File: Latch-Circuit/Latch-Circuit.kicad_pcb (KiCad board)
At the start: 4 copper layers, 0 parts

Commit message: add footprints from sch
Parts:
- added C1: 22u, ProjectEV_Capacitor:C_3216M, F.Cu at (-17.9, -17.3)
- added C2: 10n, ProjectEV_Capacitor:C_1608M, F.Cu at (-16.1, -39.3)
- added C3: 100n, ProjectEV_Capacitor:C_1608M, F.Cu at (-16.1, -37.0)
- added C4: 10n, ProjectEV_Capacitor:C_1608M, F.Cu at (-16.1, -34.6)
- added C5: 10n, ProjectEV_Capacitor:C_1608M, F.Cu at (-16.1, -32.2)
- added C6: 10n, ProjectEV_Capacitor:C_1608M, F.Cu at (-16.1, -29.9)
- added C7: 1n, ProjectEV_Capacitor:C_3216M, F.Cu at (-17.9, -14.1)
- added D1: PZ1AH11B-AU_R1_000A1, ProjectEV_Diode:PZ1AH11B-AU_R1_000A1, F.Cu at (-17.5, -10.8)
- added D2: B1911PG--20D000514U1930, ProjectEV_LED:B1911PG--20D000514U1930, F.Cu at (-41.5, -15.3)
- added D3: CUHZ20V,H3F, ProjectEV_Protection:CUHZ20V,H3F, F.Cu at (-45.8, -15.1)
- added F1: 0ABB-1000-TM, ProjectEV_Fuse:0ABB-1000-TM, F.Cu at (-46.6, -12.3)
- added H1: MountingHole_4.3mm_M4_Pad_Via, ProjectEV_Mechanical:MountingHole_4.3mm_M4_Pad_Via, F.Cu at (-53.3, -53.0)
- added H2: MountingHole_4.3mm_M4_Pad_Via, ProjectEV_Mechanical:MountingHole_4.3mm_M4_Pad_Via, F.Cu at (-53.3, -42.8)
- added H3: MountingHole_4.3mm_M4_Pad_Via, ProjectEV_Mechanical:MountingHole_4.3mm_M4_Pad_Via, F.Cu at (-53.3, -32.7)
- added H4: MountingHole_4.3mm_M4_Pad_Via, ProjectEV_Mechanical:MountingHole_4.3mm_M4_Pad_Via, F.Cu at (-53.3, -22.5)
- added J1: 2-1445052-2, ProjectEV_Connector:2-1445052-2, F.Cu at (-24.0, -21.6)
- added J2: 3-794633-8, ProjectEV_Connector:3-794633-8, F.Cu at (-22.9, -51.3)
- added J3: B2P-VH, ProjectEV_Connector_JST:B2P-VH, F.Cu at (-27.6, -14.4)
- added J4: 3-794633-6, ProjectEV_Connector:3-794633-6, F.Cu at (-31.4, -33.7)
- added Q1: DMP3098LQ-7, ProjectEV_Transistor:DMP3098LQ-7, F.Cu at (-37.0, -24.7)
- added Q2: 2N7002K-AU_R1_000A2, ProjectEV_Transistor:2N7002K-AU_R1_000A2, F.Cu at (-37.0, -20.2)
- added Q3: 2N7002K-AU_R1_000A2, ProjectEV_Transistor:2N7002K-AU_R1_000A2, F.Cu at (-37.0, -15.8)
- added Q4: 2N7002K-AU_R1_000A2, ProjectEV_Transistor:2N7002K-AU_R1_000A2, F.Cu at (-37.0, -11.3)
- added Q5: 2N7002K-AU_R1_000A2, ProjectEV_Transistor:2N7002K-AU_R1_000A2, F.Cu at (-32.5, -24.7)
- added Q6: 2N7002K-AU_R1_000A2, ProjectEV_Transistor:2N7002K-AU_R1_000A2, F.Cu at (-32.5, -20.2)
- added Q7: 2N7002K-AU_R1_000A2, ProjectEV_Transistor:2N7002K-AU_R1_000A2, F.Cu at (-32.5, -15.8)
- added R1: 10k, ProjectEV_Resistor:R_1608M, F.Cu at (-46.2, -56.8)
- added R10: 100, ProjectEV_Resistor:R_1608M, F.Cu at (-42.2, -51.8)
- added R11: 100k, ProjectEV_Resistor:R_1608M, F.Cu at (-42.2, -49.3)
- added R12: 10k, ProjectEV_Resistor:R_1608M, F.Cu at (-42.2, -46.8)
- added R13: 100, ProjectEV_Resistor:R_1608M, F.Cu at (-42.2, -44.2)
- added R14: 100k, ProjectEV_Resistor:R_1608M, F.Cu at (-42.2, -41.7)
- added R15: 10k, ProjectEV_Resistor:R_1608M, F.Cu at (-38.2, -56.8)
- added R16: 100, ProjectEV_Resistor:R_1608M, F.Cu at (-38.2, -54.3)
- added R17: 100k, ProjectEV_Resistor:R_1608M, F.Cu at (-38.2, -51.8)
- added R18: 1.2k, ProjectEV_Resistor:R_3216M, F.Cu at (-20.8, -38.8)
- added R19: 100, ProjectEV_Resistor:R_1608M, F.Cu at (-38.2, -49.3)
- added R2: 10k, ProjectEV_Resistor:R_1608M, F.Cu at (-46.2, -54.3)
- added R20: 100k, ProjectEV_Resistor:R_1608M, F.Cu at (-38.2, -46.8)
- added R21: 1.2k, ProjectEV_Resistor:R_3216M, F.Cu at (-20.8, -35.5)
- added R22: 100, ProjectEV_Resistor:R_1608M, F.Cu at (-38.2, -44.2)
- added R23: 100k, ProjectEV_Resistor:R_1608M, F.Cu at (-38.2, -41.7)
- added R24: 1.2k, ProjectEV_Resistor:R_3216M, F.Cu at (-20.8, -32.2)
- added R25: 100, ProjectEV_Resistor:R_1608M, F.Cu at (-34.2, -56.8)
- added R26: 100k, ProjectEV_Resistor:R_1608M, F.Cu at (-34.2, -54.3)
- added R27: 1M, ProjectEV_Resistor:R_3216M, F.Cu at (-20.8, -29.0)
- added R28: 0, ProjectEV_Resistor:R_1608M, F.Cu at (-34.2, -51.8)
- added R29: 0, ProjectEV_Resistor:R_1608M, F.Cu at (-34.2, -49.3)
- added R3: 0, ProjectEV_Resistor:R_1608M, F.Cu at (-46.2, -51.8)
- added R30: 0, ProjectEV_Resistor:R_1608M, F.Cu at (-34.2, -46.8)
- added R4: 0, ProjectEV_Resistor:R_1608M, F.Cu at (-46.2, -49.3)
- added R5: 0, ProjectEV_Resistor:R_1608M, F.Cu at (-46.2, -46.8)
- added R6: 0, ProjectEV_Resistor:R_1608M, F.Cu at (-46.2, -44.2)
- added R7: 100, ProjectEV_Resistor:R_1608M, F.Cu at (-46.2, -41.7)
- added R8: 10k, ProjectEV_Resistor:R_1608M, F.Cu at (-42.2, -56.8)
- added R9: 10k, ProjectEV_Resistor:R_1608M, F.Cu at (-42.2, -54.3)
- added U1: TLP3106A(TP,F, ProjectEV_Relay:TLP3106A(TP,F, F.Cu at (-43.7, -36.4)
- added U2: TLP3106A(TP,F, ProjectEV_Relay:TLP3106A(TP,F, F.Cu at (-43.7, -28.4)
- added U3: TLP3106A(TP,F, ProjectEV_Relay:TLP3106A(TP,F, F.Cu at (-43.7, -20.4)
- added U4: CD4043BPWR, ProjectEV_Logic:CD4043BPWR, F.Cu at (-53.6, -14.1)

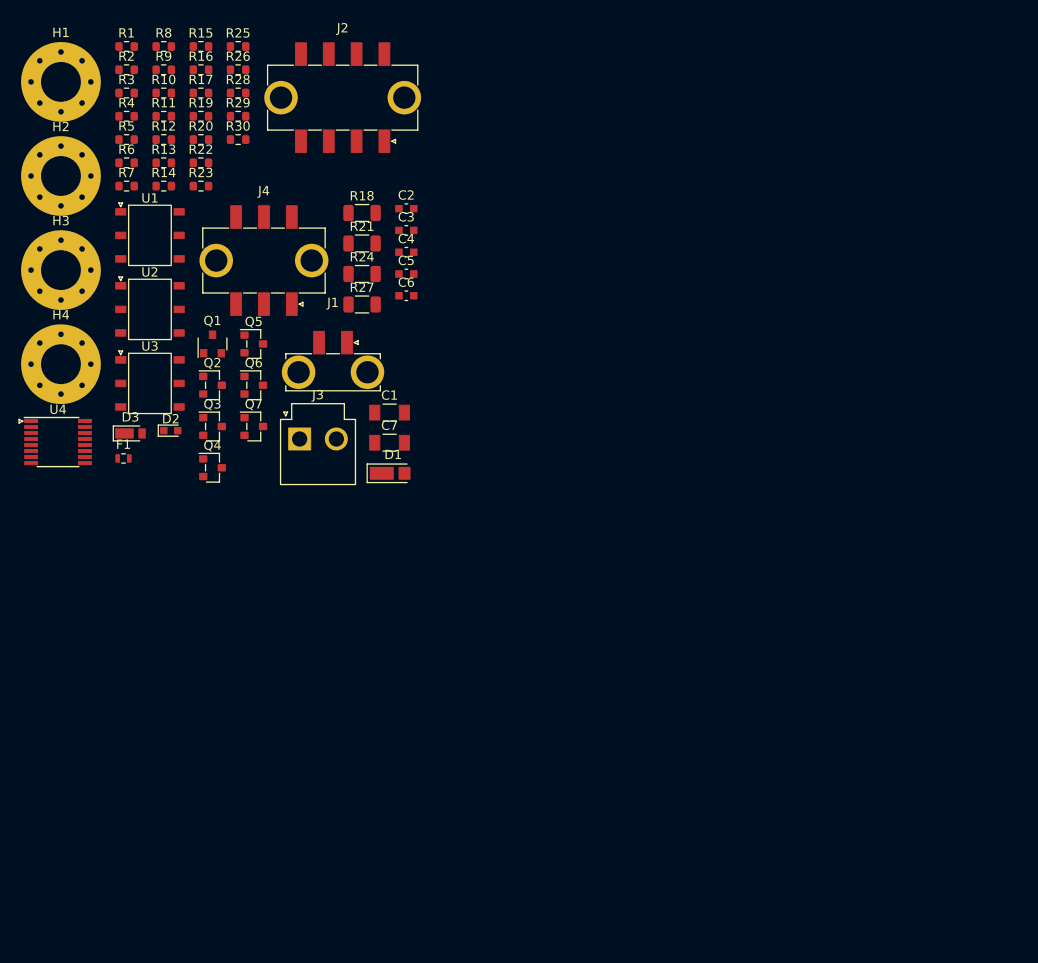
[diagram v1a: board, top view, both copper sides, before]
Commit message: update footprints, and place components
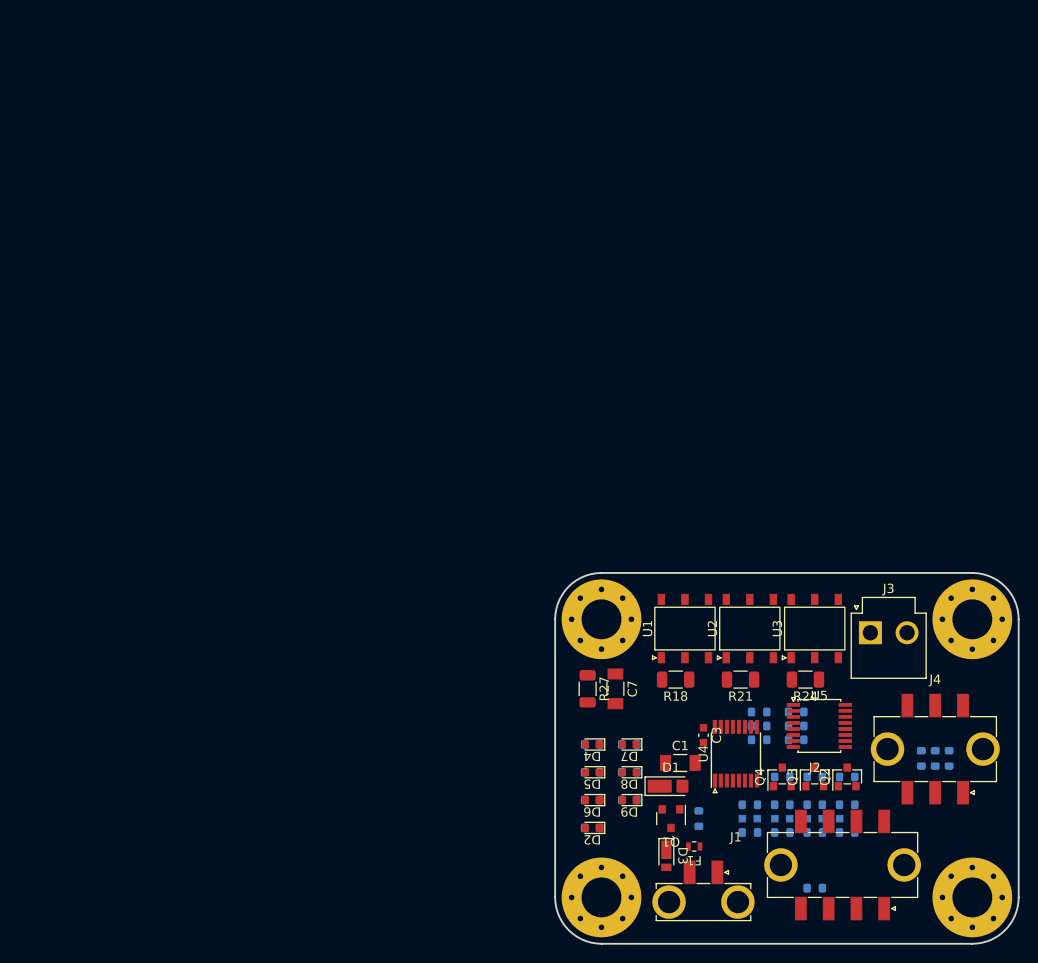
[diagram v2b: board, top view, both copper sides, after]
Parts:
- removed Q5, Q6, Q7: 2N7002K-AU_R1_000A2, ProjectEV_Transistor:2N7002K-AU_R1_000A2
- added D4: B1911PG--20D000514U1930, ProjectEV_LED:B1911PG--20D000514U1930, F.Cu at (4.00, 18.5)
- added D5: B1911PG--20D000514U1930, ProjectEV_LED:B1911PG--20D000514U1930, F.Cu at (4.00, 21.5)
- added D6: B1911PG--20D000514U1930, ProjectEV_LED:B1911PG--20D000514U1930, F.Cu at (4.00, 24.5)
- added D7: B1911USD-20D000114U1930, ProjectEV_LED:B1911USD-20D000114U1930, F.Cu at (8.00, 18.5)
- added D8: B1911USD-20D000114U1930, ProjectEV_LED:B1911USD-20D000114U1930, F.Cu at (8.00, 21.5)
- added D9: B1911USD-20D000114U1930, ProjectEV_LED:B1911USD-20D000114U1930, F.Cu at (8.00, 24.5)
- added R31: 10k, ProjectEV_Resistor:R_1608M, B.Cu at (4.00, 18.5)
- added R32: 10k, ProjectEV_Resistor:R_1608M, B.Cu at (4.00, 21.5)
- added R33: 10k, ProjectEV_Resistor:R_1608M, B.Cu at (4.00, 24.5)
- added U5: TBD62003AFNG,EL, ProjectEV_PowerManagement:TBD62003AFNG,EL, F.Cu at (28.5, 16.5)
- C2, C4, C5, C6, R1, R10, R11, R12, R13, R14, R15, R16, R17, R19, R2, R20, R22, R23, R25, R26, R3, R4, R5, R6, R7, R8, R9: moved to B.Cu
- R28, R29, R30: value 0 -> 10k; moved to B.Cu
- moved H3 119.3 mm to (45.0, 35.0)
- moved R3 114.1 mm to (42.5, 20.0), turned to 90 degrees
- moved R4 111.4 mm to (41.0, 20.0), turned to 90 degrees
- moved R5 108.7 mm to (39.5, 20.0), turned to 90 degrees
- moved R10 108.6 mm to (31.5, 28.0)
- moved R6 107.8 mm to (28.0, 34.0), turned to 180 degrees
- moved R9 106.1 mm to (31.5, 22.0), turned to 180 degrees
- moved R11 104.6 mm to (31.5, 25.0)
- moved R1 103.7 mm to (15.5, 26.5), turned to -90 degrees
- moved R16 103.5 mm to (24.5, 28.0)
- moved R8 103.4 mm to (21.0, 25.0)
- moved H4 102.1 mm to (45.0, 5.00)
- moved R13 100.7 mm to (28.0, 28.0)
- moved R15 100.7 mm to (24.5, 22.0)
- moved R17 99.1 mm to (24.5, 25.0)
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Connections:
- J4 pad 4: /BMS_LED_K -> BMS_LED_K
- J4 pad 5: /BSPD_LED_K -> BSPD_LED_K
- J4 pad 6: /IMD_LED_K -> IMD_LED_K
- R28 pad 1: BMS_RLY_OFF -> Net-(D7-A)
- R28 pad 2: /BMS_LED_K -> +12V
- R29 pad 1: BSPD_RLY_OFF -> Net-(D8-A)
- R29 pad 2: /BSPD_LED_K -> +12V
- R30 pad 1: IMD_RLY_OFF -> Net-(D9-A)
- R30 pad 2: /IMD_LED_K -> +12V
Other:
- board outline added: 50 x 40 mm

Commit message: finish wiring
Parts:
- moved D1 4.30 mm to (16.0, 25.5)
- moved C1 3.91 mm to (16.5, 23.0)
- moved R1 3.50 mm to (19.0, 26.5)
- moved Q1 3.20 mm to (15.0, 28.5)
- moved D2 3.00 mm to (7.00, 27.5)
- moved D4 3.00 mm to (7.00, 18.5)
- moved D5 3.00 mm to (7.00, 21.5)
- moved D6 3.00 mm to (7.00, 24.5)
- moved D7 3.00 mm to (11.0, 18.5)
- moved D8 3.00 mm to (11.0, 21.5)
- moved D9 3.00 mm to (11.0, 24.5)
- moved F1 3.00 mm to (18.0, 29.5)
- moved R2 3.00 mm to (7.00, 27.5)
- moved R28 3.00 mm to (11.0, 18.5)
- moved R29 3.00 mm to (11.0, 21.5)
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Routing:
- net +12V: track 0.00 -> 53.5 mm, vias 0 -> 20
- net ~{BMS_STATUS}: track 0.00 -> 46.3 mm, vias 0 -> 2
- net BMS_LED_K: track 0.00 -> 40.1 mm, vias 0 -> 2
- net BSPD_LED_K: track 0.00 -> 35.9 mm, vias 0 -> 2
- net ~{IMD_STATUS}: track 0.00 -> 34.8 mm, vias 0 -> 2
- net ~{BSPD_STATUS}: track 0.00 -> 32.7 mm, vias 0 -> 2
- net IMD_LED_K: track 0.00 -> 32.6 mm, vias 0 -> 2
- net BMS_RLY_OFF: track 0.00 -> 24.1 mm, vias 0 -> 2
- net IMD_RLY_OFF: track 0.00 -> 21.3 mm, vias 0 -> 2
- net RST: track 0.00 -> 19.9 mm, vias 0 -> 1
- net BSPD_RLY_OFF: track 0.00 -> 17.4 mm, vias 0 -> 2
- net BMS_FAULT: track 0.00 -> 6.85 mm, vias 0 -> 1
- net BSPD_FAULT: track 0.00 -> 6.54 mm, vias 0 -> 1
- net Net-(U5-I5): track 0.00 -> 6.26 mm, vias 0 -> 1
- net BSPD_STATUS: track 0.00 -> 6.04 mm, vias 0 -> 1
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- added copper zone on F.Cu, net +12V
- added copper zone on In2.Cu, net +12V
- added copper zone on F.Cu, net /GLV_IN
- added copper zone on F.Cu, net /SHDN_IN
- added copper zone on F.Cu, net /SHDN_OUT
- added copper zone on B.Cu, net Chassis
- added copper zone on F.Cu, net Chassis
- added copper zone on In1.Cu, net Chassis
- added copper zone on In2.Cu, net Chassis
- added copper zone on B.Cu, net GND
- added copper zone on F.Cu, net GND
- added copper zone on In1.Cu, net GND
- added copper zone on In2.Cu, net GND
- added copper zone on F.Cu, net Net-(D3-K)
- added copper zone on F.Cu, net Net-(U1-Drain-Pad4)
- added copper zone on F.Cu, net Net-(U2-Drain-Pad4)
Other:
- board text added: "BMS"
- board text added: "BSPD"
- board text added: "FLT"
- board text added: "IMD"
- board text added: "IN"
- board text added: "PWR"

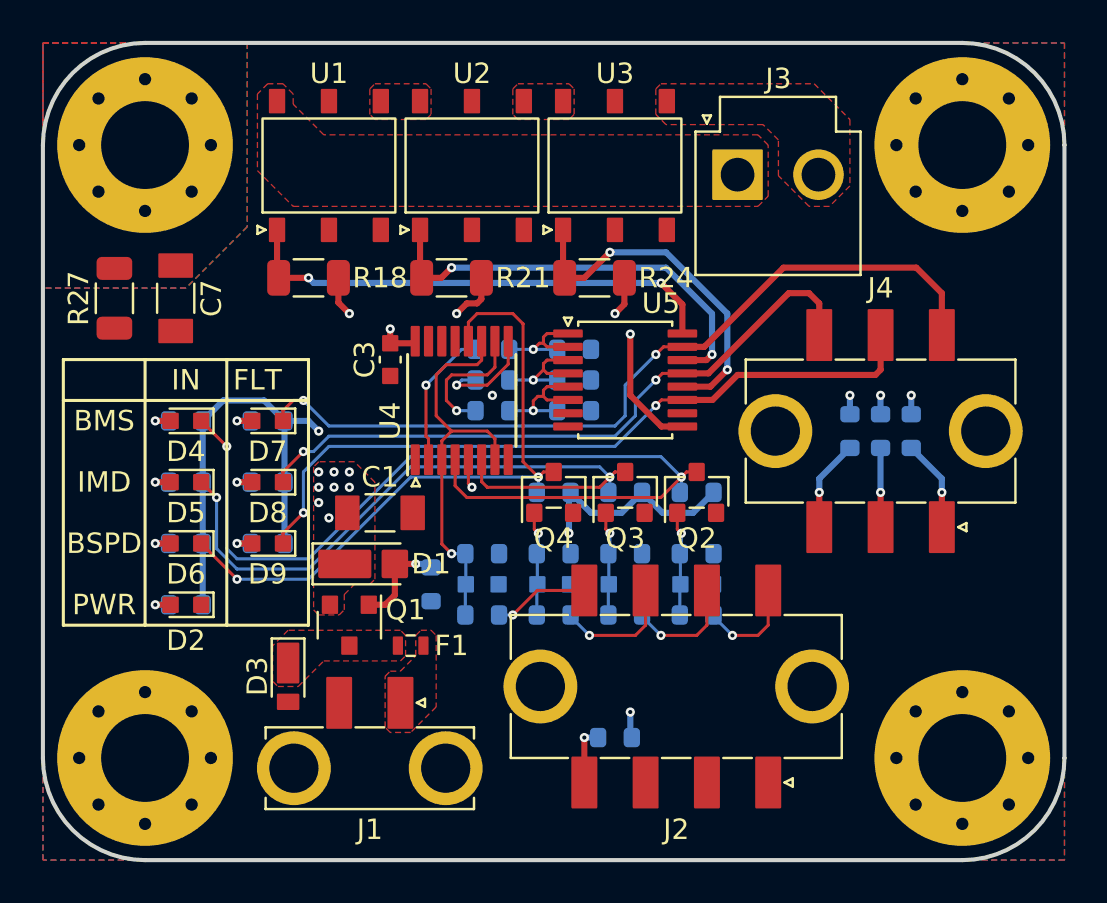
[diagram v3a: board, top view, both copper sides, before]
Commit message: add vias
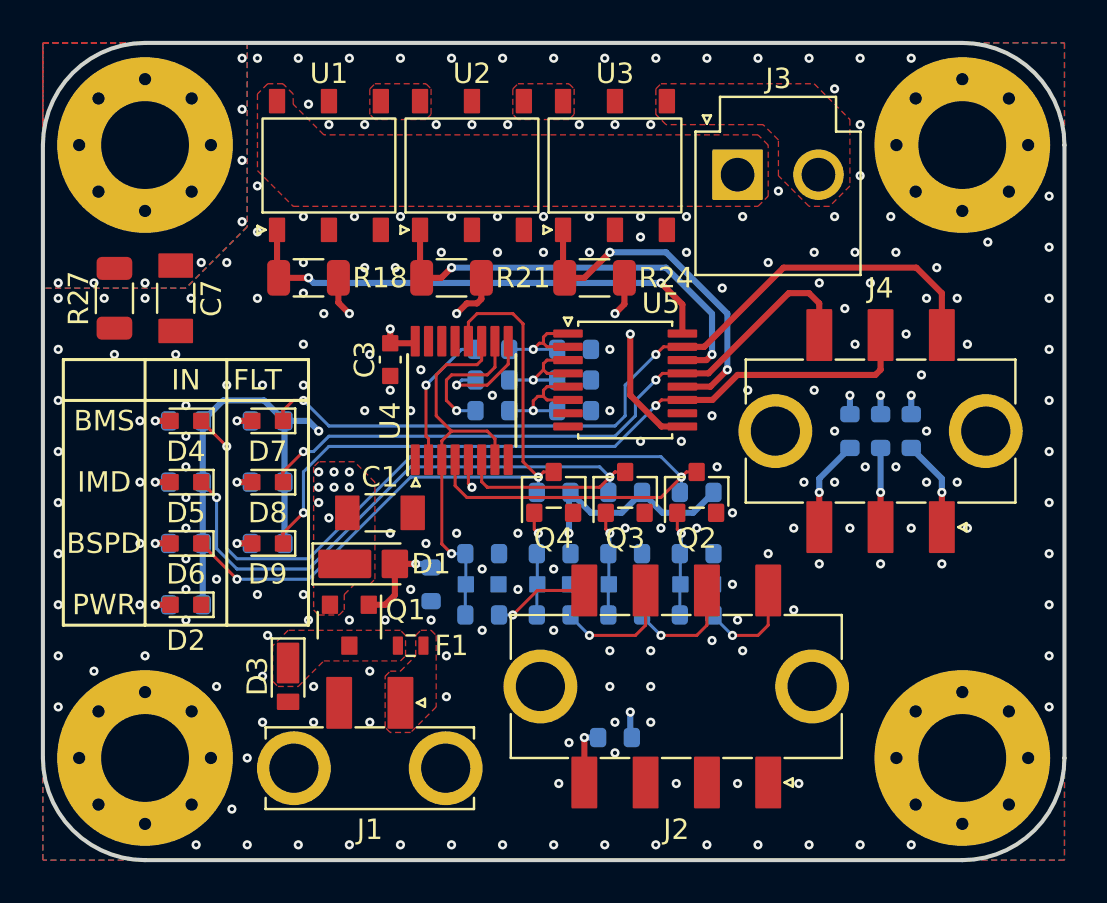
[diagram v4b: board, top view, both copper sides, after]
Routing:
- net GND: vias 1 -> 208
- net Chassis: vias 0 -> 8
